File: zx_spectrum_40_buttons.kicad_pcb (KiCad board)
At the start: 2 copper layers, 220 x 90 mm, 42 parts, among them J1 column, J2 str, SW1 1, SW10 E, SW11 D, SW12 X, SW13 4, SW14 R, SW15 F, SW16 C, SW17 5, SW18 T, SW19 G, SW2 Q, SW20 V, SW21 6, SW22 Y, SW23 H, SW24 B, SW25 7, SW26 U, SW27 J, SW28 N, SW29 8, SW3 A, SW30 I, SW31 K, SW32 M, SW33 9, SW34 O, SW35 L, SW36 S.S., SW37 10, SW38 P, SW39 ENTER, SW4 C.S., SW40 SPACE, SW5 2, SW6 W, SW7 S, SW8 Z, SW9 3

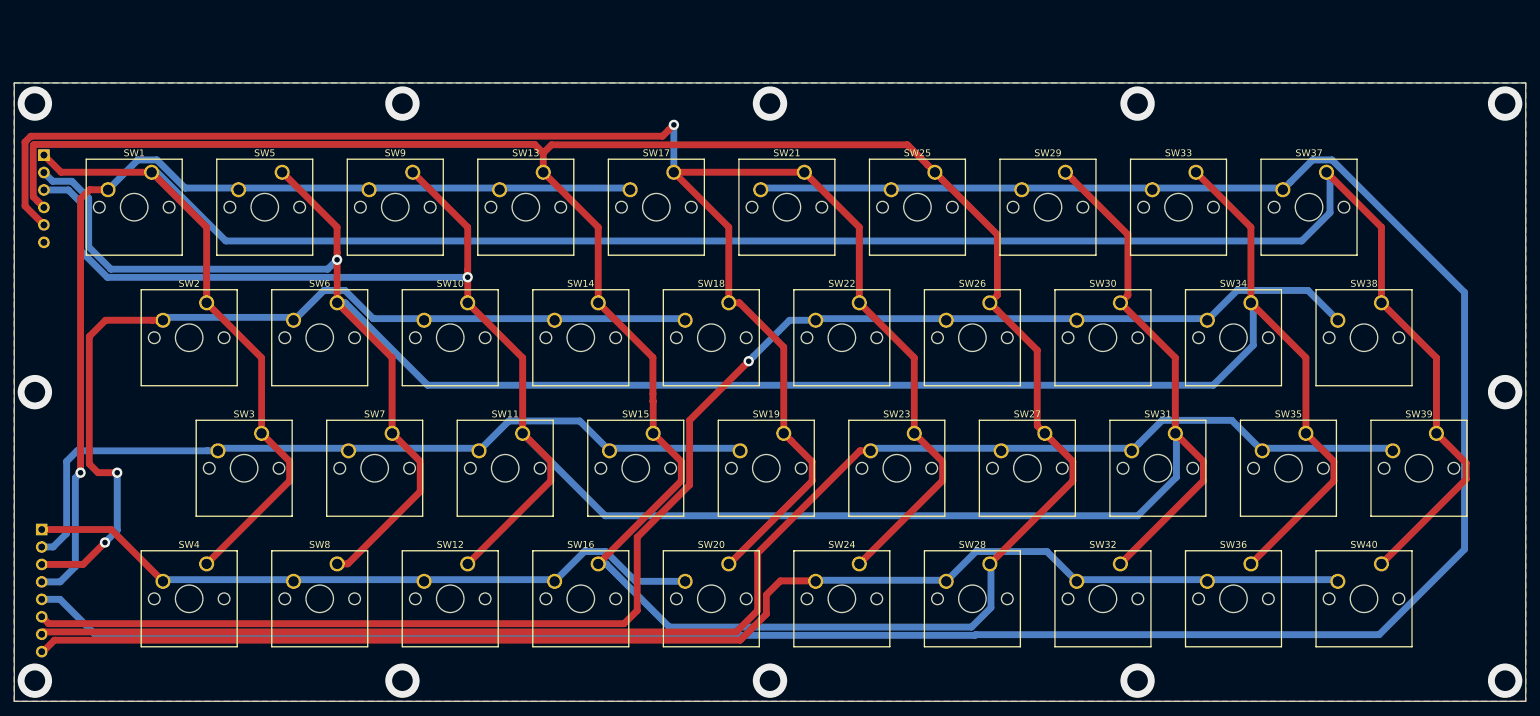
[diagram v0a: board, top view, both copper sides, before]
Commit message: +10 см снизу для креплений.
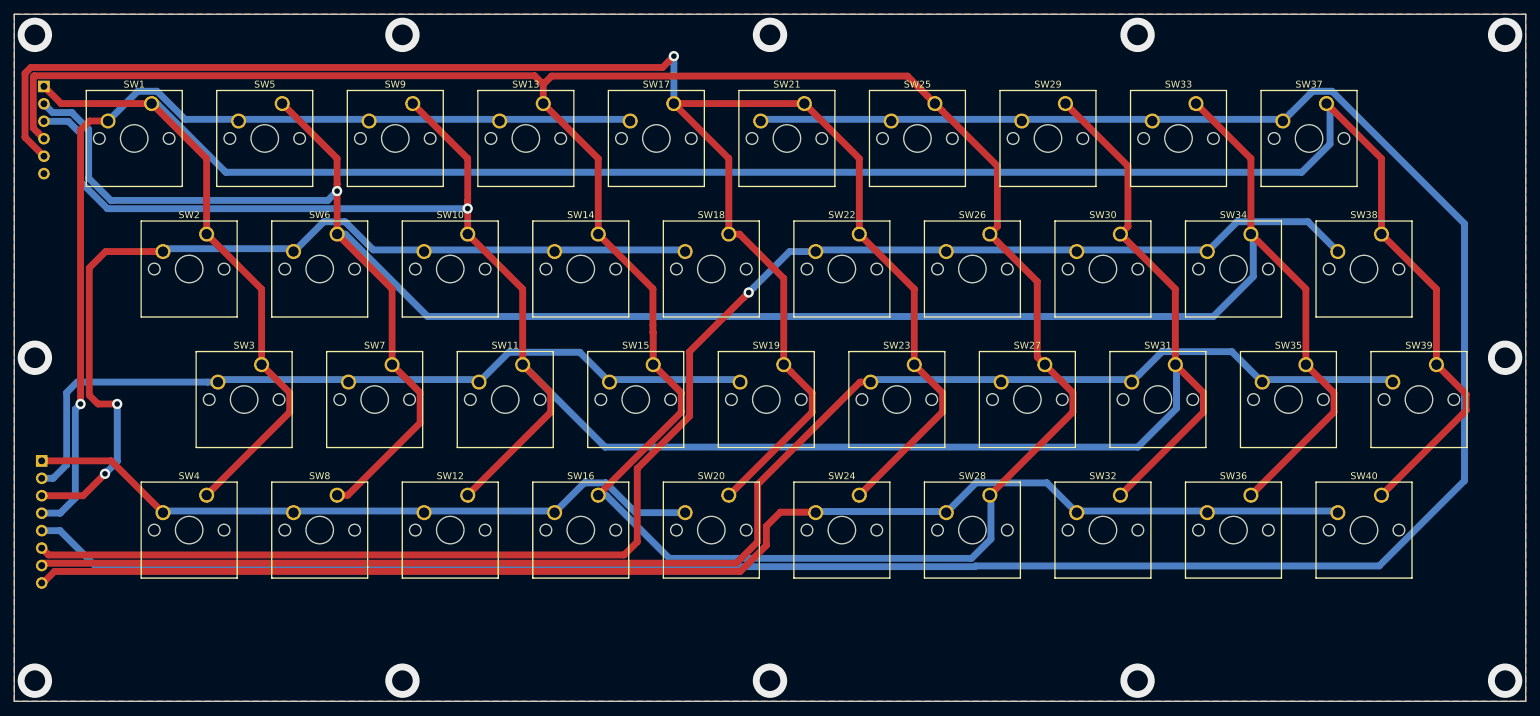
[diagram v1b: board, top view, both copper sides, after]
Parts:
- moved J1 10.0 mm to (35.3, 50.5)
- moved J2 10.0 mm to (35.0, 105.0)
- moved SW1 10.0 mm to (51.0, 53.0)
- moved SW10 10.0 mm to (97.0, 72.0)
- moved SW11 10.0 mm to (105.0, 91.0)
- moved SW12 10.0 mm to (97.0, 110.0)
- moved SW13 10.0 mm to (108.0, 53.0)
- moved SW14 10.0 mm to (116.0, 72.0)
- moved SW15 10.0 mm to (124.0, 91.0)
- moved SW16 10.0 mm to (116.0, 110.0)
- moved SW17 10.0 mm to (127.0, 53.0)
- moved SW18 10.0 mm to (135.0, 72.0)
- moved SW19 10.0 mm to (143.0, 91.0)
- moved SW2 10.0 mm to (59.0, 72.0)
- moved SW20 10.0 mm to (135.0, 110.0)
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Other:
- board size 220 x 90 mm -> 220 x 100 mm
